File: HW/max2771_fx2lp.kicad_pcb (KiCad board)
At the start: 4 copper layers, 40.5 x 36.8 mm, 53 parts, among them J1 SMA-ANG, J2 SMA-ANG, J3 Screw_Terminal_01x02, J4 SMA-ANG, P1 Conn_02x10_Odd_Even, P2 Conn_02x10_Odd_Even, U1 MAX2771, U2 MAX2771

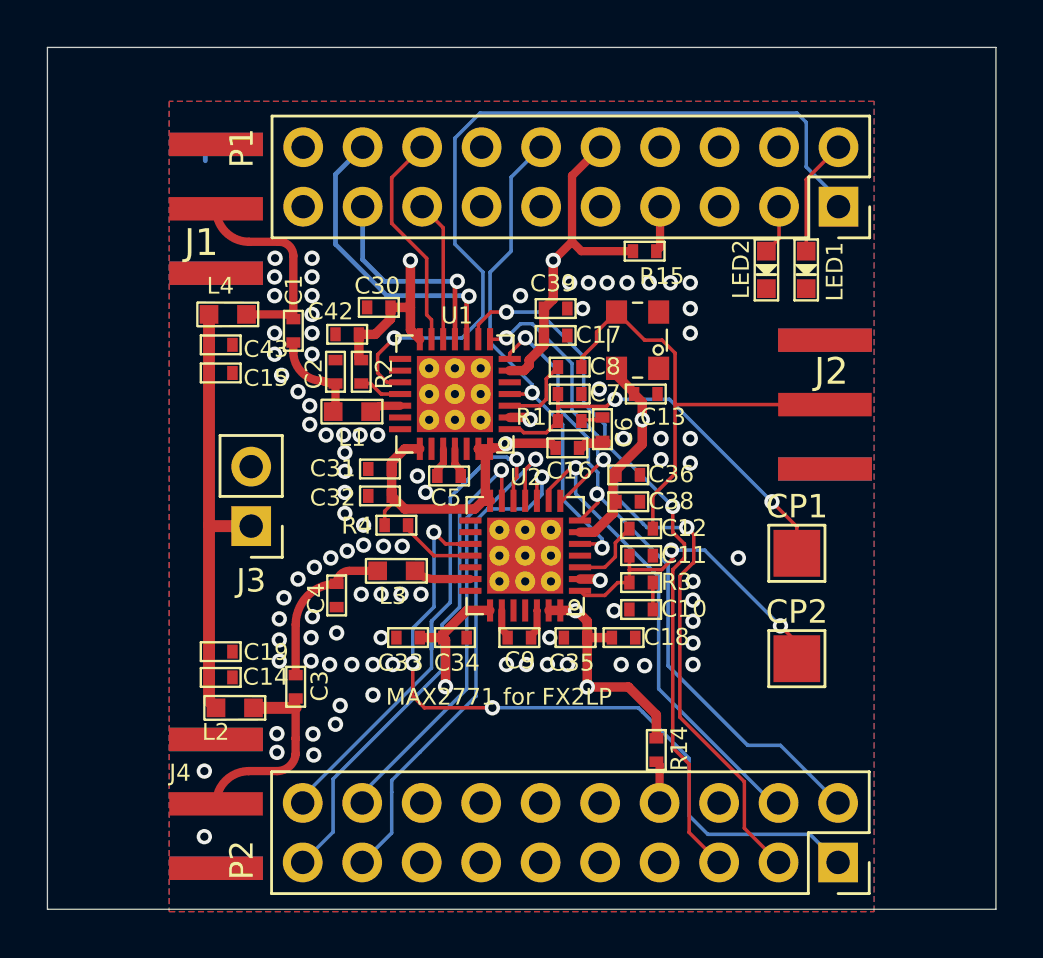
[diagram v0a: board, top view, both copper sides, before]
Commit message: add option for feeding either Hi or Lo frequency band
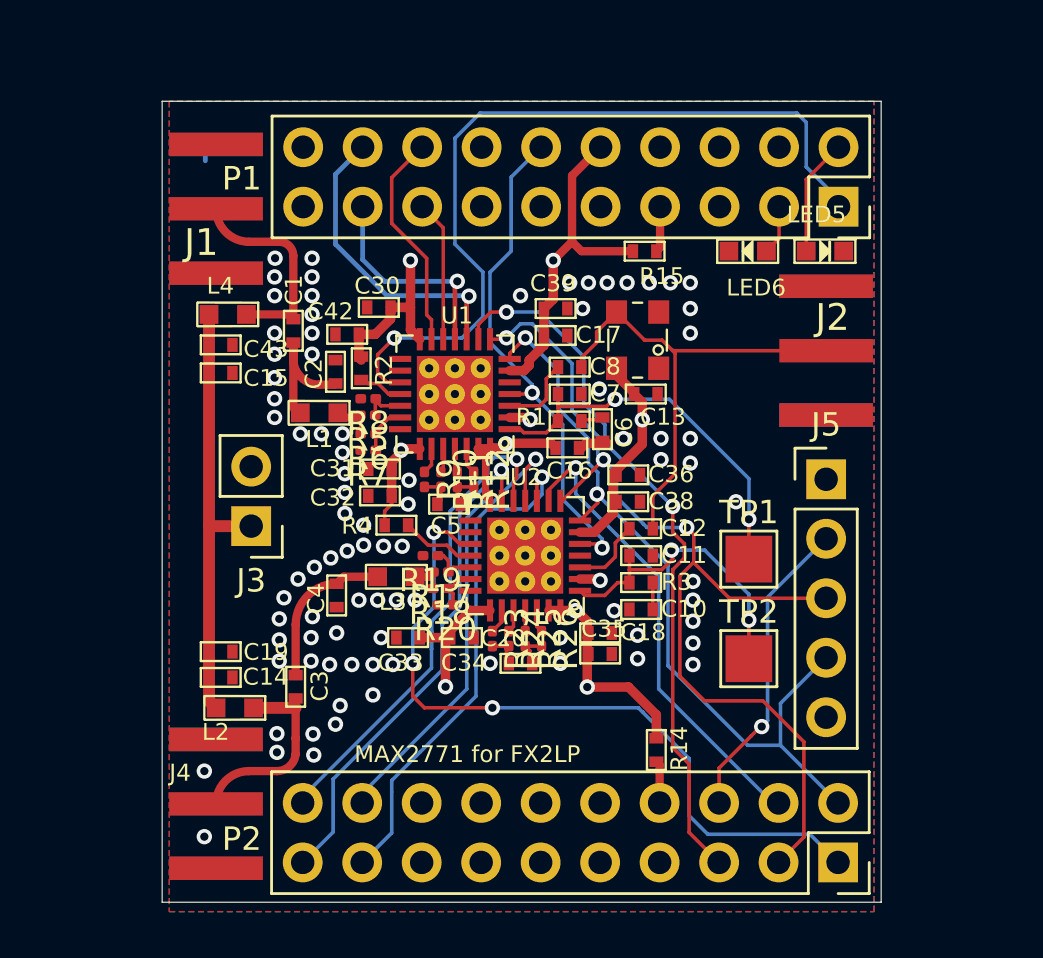
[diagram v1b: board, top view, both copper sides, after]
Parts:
- removed C9: 470pF, pocket_sdr_v2.3:C1005
- removed CP1, CP2: TestPoint, TestPoint:TestPoint_Pad_2.0x2.0mm
- removed LED1, LED2: LED1608, pocket_sdr_v2.3:LED_1608
- added C20: 470pF, pocket_sdr_v2.3:C1005, F.Cu at (141.2, 114.0)
- added J5: Conn_01x05_Pin, Connector_PinHeader_2.54mm:PinHeader_1x05_P2.54mm_Vertical, F.Cu at (154.3, 106.2)
- added LED5: LED1608, pocket_sdr_v2.3:LED_1608, F.Cu at (154.2, 96.5)
- added LED6: LED1608, pocket_sdr_v2.3:LED_1608, F.Cu at (150.9, 96.5)
- added R10: 0hi nclo, Resistor_SMD:R_0201_0603Metric, F.Cu at (137.8, 106.2)
- added R11: 0hi nclo, Resistor_SMD:R_0201_0603Metric, F.Cu at (138.5, 106.2)
- added R12: 0lo nchi, Resistor_SMD:R_0201_0603Metric, F.Cu at (139.2, 106.2)
- added R17: 0hi nclo, Resistor_SMD:R_0201_0603Metric, F.Cu at (137.8, 110.2)
- added R18: 0lo nchi, Resistor_SMD:R_0201_0603Metric, F.Cu at (137.8, 110.8)
- added R19: 0lo nchi, Resistor_SMD:R_0201_0603Metric, F.Cu at (137.4, 109.5)
- added R20: 0hi nclo, Resistor_SMD:R_0201_0603Metric, F.Cu at (138.0, 111.5)
- added R23: 0lo nchi, Resistor_SMD:R_0201_0603Metric, F.Cu at (140.0, 113.0)
- added R24: 0hi nclo, Resistor_SMD:R_0201_0603Metric, F.Cu at (140.7, 113.0)
- added R25: 0hi nclo, Resistor_SMD:R_0201_0603Metric, F.Cu at (141.4, 113.0)
- added R26: 0lo nchi, Resistor_SMD:R_0201_0603Metric, F.Cu at (142.1, 113.0)
- added R5: 0hi nclo, Resistor_SMD:R_0201_0603Metric, F.Cu at (134.7, 103.5)
- added R6: 0lo nchi, Resistor_SMD:R_0201_0603Metric, F.Cu at (134.7, 104.2)
- added R7: 0hi nclo, Resistor_SMD:R_0201_0603Metric, F.Cu at (134.7, 105.0)
- added R8: 0lo nchi, Resistor_SMD:R_0201_0603Metric, F.Cu at (134.7, 102.8)
- added R9: 0lo nchi, Resistor_SMD:R_0201_0603Metric, F.Cu at (137.1, 106.2)
- added TP1: TestPoint, TestPoint:TestPoint_Pad_2.0x2.0mm, F.Cu at (151.0, 109.6)
- added TP2: TestPoint, TestPoint:TestPoint_Pad_2.0x2.0mm, F.Cu at (151.0, 113.8)
- moved J2 2.30 mm to (158.3, 100.7)
- moved L1 1.40 mm to (132.6, 103.3)
- moved C35 1.26 mm to (144.6, 113.7), turned to 0 degrees
- moved C5 1.20 mm to (138.2, 107.2)
- moved C18 1.02 mm to (144.6, 112.8)
- moved C34 0.30 mm to (138.7, 113.0)
- moved L3 0.25 mm to (135.9, 110.3)
- moved R2 0.15 mm to (134.4, 101.5)
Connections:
- C5 pad 1: Net-(U1-LNAOUT_HI) -> Net-(R10-P$2)
- C5 pad 2: Net-(U1-MIXIN_HI) -> Net-(R11-P$2)
- P2 pad 6: unconnected-(P2-Pin_6-Pad6) -> PA7
- U1 pad 19: Net-(L1-P$2) -> Net-(R5-P$1)
- U1 pad 20: CPAD_2.2MM -> Net-(R6-P$1)
- U1 pad 23: unconnected-(U1-LNAOUT_LO-Pad23) -> Net-(R9-P$1)
- U1 pad 24: Net-(U1-LNAOUT_HI) -> Net-(R10-P$1)
- U1 pad 25: Net-(U1-MIXIN_HI) -> Net-(R11-P$1)
- U1 pad 26: CPAD_2.2MM -> Net-(R12-P$1)
- U2 pad 19: CPAD_2.2MM -> Net-(R17-P$1)
- U2 pad 20: Net-(L3-P$2) -> Net-(R18-P$1)
- U2 pad 24: unconnected-(U2-LNAOUT_HI-Pad24) -> Net-(R24-P$1)
- U2 pad 25: CPAD_2.2MM -> Net-(R25-P$1)
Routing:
- net PA7: track 0.00 -> 13.3 mm, vias 0 -> 1
- net SCLK: track 33.7 -> 42.3 mm
- net SDATA: track 28.9 -> 33.4 mm
- net +3.3V: track 125.3 -> 129.3 mm, vias 9 -> 10
- net Net-(L1-P$1): track 4.10 -> 6.27 mm
- net Net-(R6-P$1): track 0.00 -> 2.10 mm
- net Net-(R18-P$1): track 0.00 -> 2.06 mm
- net Net-(R17-P$1): track 0.00 -> 2.04 mm
- net Net-(R5-P$1): track 0.00 -> 1.97 mm
- net I0_B: track 24.2 -> 22.3 mm
- net Net-(R25-P$2): track 0.00 -> 1.52 mm
- net Net-(R11-P$2): track 0.00 -> 1.50 mm
- net Net-(R10-P$2): track 0.00 -> 1.50 mm
- net Net-(R23-P$2): track 0.00 -> 1.48 mm
- net Net-(U1-LNAOUT_HI): track 1.27 -> 0.00 mm
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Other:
- board size 40.5 x 36.8 mm -> 30.7 x 34.2 mm
